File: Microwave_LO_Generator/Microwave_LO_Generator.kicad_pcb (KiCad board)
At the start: 2 copper layers, 41 parts, among them IC1 ADP150AUJZ-3.3-R7, J1 BNC_THT, J2 SMA_END, J3 SMA_END, U1 ADF4150HV, U2 LM317L_SO8, U3 LM317L_SO8, X1 IQXT-220-1

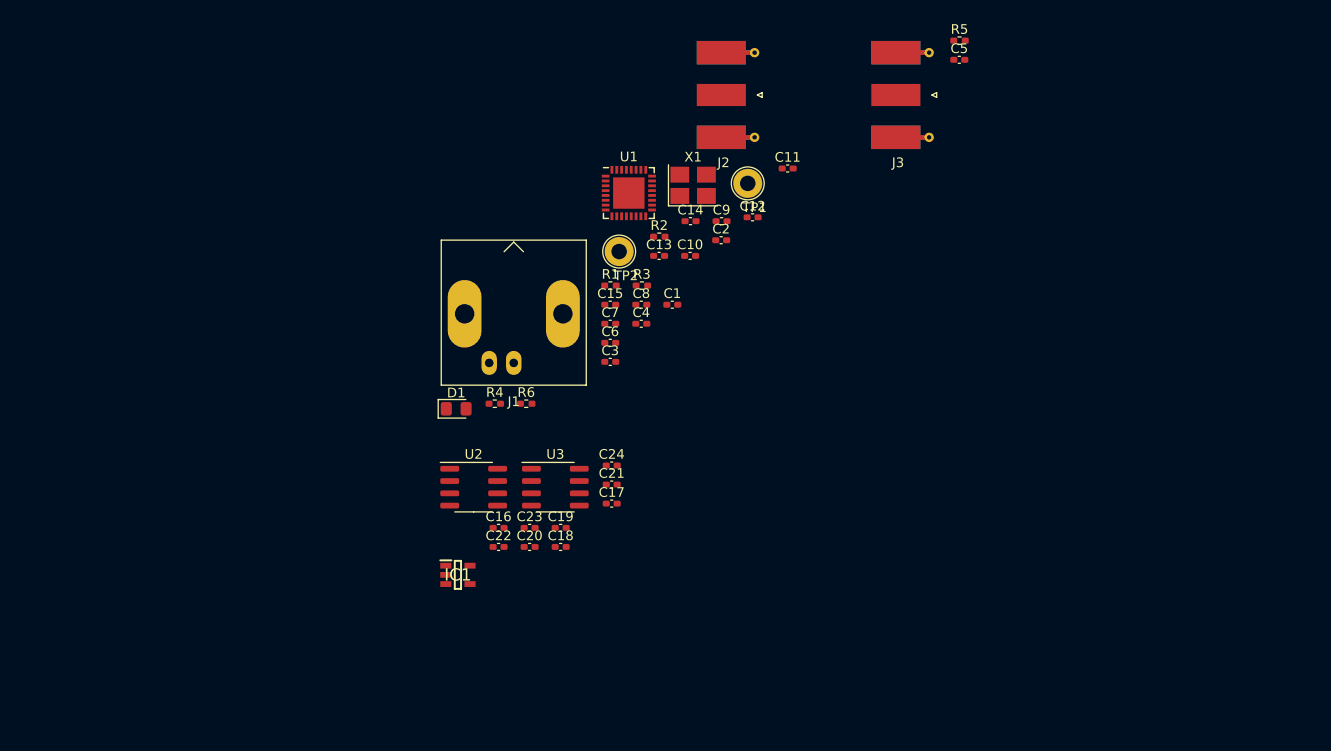
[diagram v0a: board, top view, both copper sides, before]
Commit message: add vco
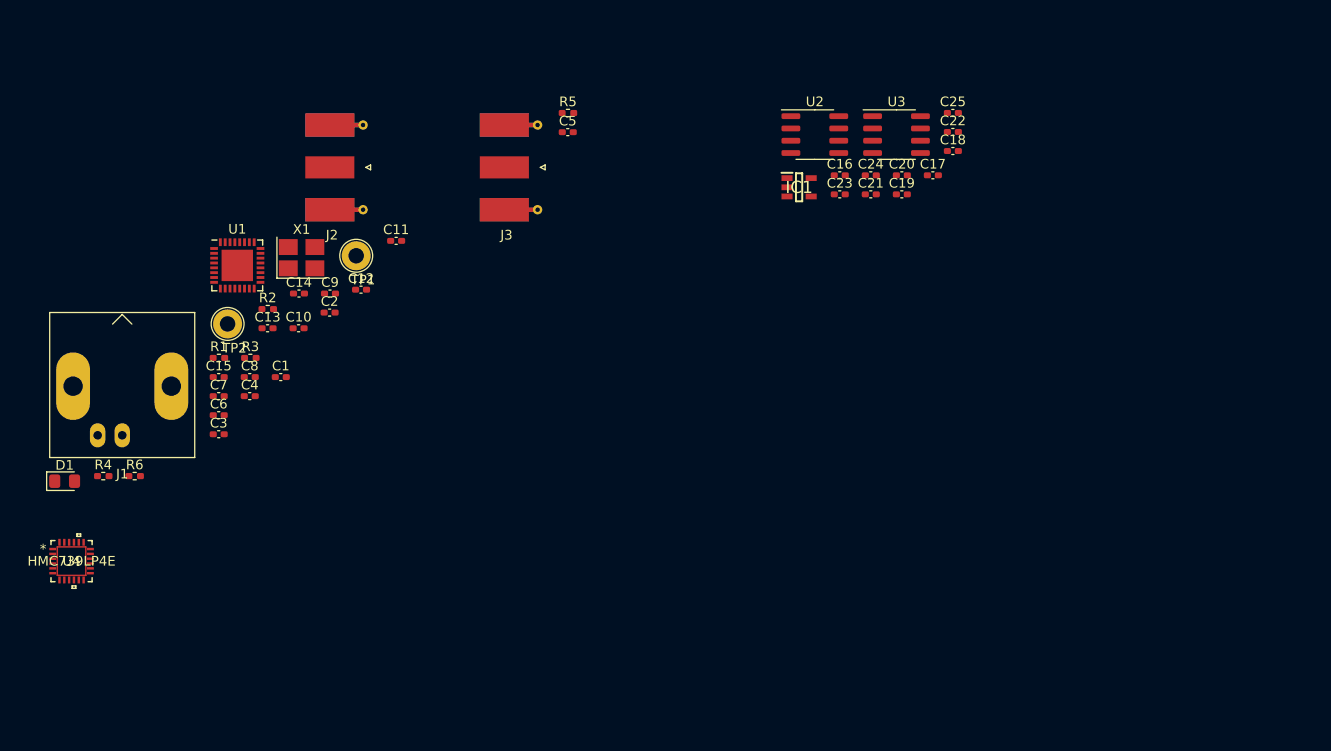
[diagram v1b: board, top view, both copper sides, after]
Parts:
- added C25: 1u, Capacitor_SMD:C_0402_1005Metric_Pad0.74x0.62mm_HandSolder, F.Cu at (236.0, 98.3)
- added U4: HMC739LP4E, Microwave_LO_Generator:HMC739LP4E, F.Cu at (144.9, 144.6)
- moved C22 63.6 mm to (236.0, 100.2)
- moved C18 57.6 mm to (236.0, 102.2)
- moved C20 54.4 mm to (230.7, 104.7)
- moved IC1 53.4 mm to (220.1, 106.0)
- moved C16 50.7 mm to (224.3, 104.7)
- moved U2 50.7 mm to (221.7, 100.5)
- moved U3 50.7 mm to (230.2, 100.5)
- moved C19 49.3 mm to (230.7, 106.7)
- moved C17 47.5 mm to (234.0, 104.7)
- moved C23 47.1 mm to (224.3, 106.7)
- moved C12 41.2 mm to (174.8, 116.6)
- moved D1 41.2 mm to (144.2, 136.4)
- moved J1 41.2 mm to (150.1, 131.6)
- moved R1 41.2 mm to (160.1, 123.6)
- moved R3 41.2 mm to (163.4, 123.6)
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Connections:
- net Net-(C15-Pad2) renamed CPout
- IC1 pad 4: Net-(IC1-Pad4) -> +5VD

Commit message: Update and fix
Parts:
- added C26: 100p, Capacitor_SMD:C_0402_1005Metric_Pad0.74x0.62mm_HandSolder, F.Cu at (263.5, 121.3)
- added C27: 4.7u, Capacitor_SMD:C_0402_1005Metric_Pad0.74x0.62mm_HandSolder, F.Cu at (262.3, 121.3)
- added C28: 1000p, Capacitor_SMD:C_0402_1005Metric_Pad0.74x0.62mm_HandSolder, F.Cu at (251.2, 118.0)
- added C29: 100p, Capacitor_SMD:C_0402_1005Metric_Pad0.74x0.62mm_HandSolder, F.Cu at (268.7, 116.2)
- added C30: 4.7u, Capacitor_SMD:C_0402_1005Metric_Pad0.74x0.62mm_HandSolder, F.Cu at (268.6, 114.3)
- added D2: DIODE, Diode_SMD:D_MELF, F.Cu at (202.1, 137.8)
- added D3: DIODE, Diode_SMD:D_MELF, F.Cu at (218.4, 134.6)
- added D4: DIODE, Diode_SMD:D_MELF, F.Cu at (218.4, 150.5)
- added D5: DIODE, Diode_SMD:D_MELF, F.Cu at (219.1, 142.9)
- added D6: DIODE, Diode_SMD:D_MELF, F.Cu at (219.1, 158.8)
- added D7: LED, LED_SMD:LED_0805_2012Metric_Pad1.15x1.40mm_HandSolder, F.Cu at (188.6, 147.3)
- added R10: 720r, Resistor_SMD:R_0402_1005Metric_Pad0.72x0.64mm_HandSolder, F.Cu at (224.8, 140.3)
- added R11: 240r, Resistor_SMD:R_0402_1005Metric_Pad0.72x0.64mm_HandSolder, F.Cu at (219.7, 156.2)
- added R12: 1K488, Resistor_SMD:R_0402_1005Metric_Pad0.72x0.64mm_HandSolder, F.Cu at (224.8, 156.2)
- added R13: 1K, Resistor_SMD:R_0402_1005Metric_Pad0.72x0.64mm_HandSolder, F.Cu at (187.3, 144.8)
- added R14: 51r, Resistor_SMD:R_0402_1005Metric_Pad0.72x0.64mm_HandSolder, F.Cu at (249.2, 117.4)
- added R15: 51r, Resistor_SMD:R_0402_1005Metric_Pad0.72x0.64mm_HandSolder, F.Cu at (267.3, 125.1)
- added R7: 0r, Resistor_SMD:R_0402_1005Metric_Pad0.72x0.64mm_HandSolder, F.Cu at (212.7, 132.1)
- added R8: 0r, Resistor_SMD:R_0402_1005Metric_Pad0.72x0.64mm_HandSolder, F.Cu at (212.7, 148.0)
- added R9: 240r, Resistor_SMD:R_0402_1005Metric_Pad0.72x0.64mm_HandSolder, F.Cu at (219.7, 140.3)
- C23: value 1u -> 4.7u
- C24: value 1u -> 100p
- moved U4 124.9 mm to (267.3, 120.0)
- moved R6 103.6 mm to (253.9, 120.5), turned to 180 degrees
- moved C15 96.5 mm to (256.5, 121.1), turned to 90 degrees
- moved D1 91.5 mm to (234.3, 120.7), turned to 90 degrees
- moved R4 89.2 mm to (235.6, 118.1)
- moved C6 88.2 mm to (247.3, 116.2), turned to 270 degrees
- moved C8 85.4 mm to (248.5, 119.3), turned to 180 degrees
- moved C7 84.6 mm to (242.6, 108.6)
- moved C13 83.4 mm to (248.5, 121.1), turned to 90 degrees
- moved C14 82.7 mm to (250.8, 123.6), turned to 90 degrees
- moved U1 80.1 mm to (241.9, 118.7), turned to 90 degrees
- moved R1 76.5 mm to (236.2, 115.6)
- moved C10 75.4 mm to (243.8, 122.6), turned to 180 degrees
- moved C4 75.0 mm to (237.5, 116.8), turned to 180 degrees
- moved R3 74.2 mm to (237.5, 121.3), turned to 270 degrees
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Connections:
- net Net-(C5-Pad2) renamed DIV16
- C1 pad 1: GND -> 0
- C10 pad 1: GND -> 0
- C11 pad 1: GND -> 0
- C12 pad 1: GND -> 0
- C13 pad 1: GND -> 0
- C14 pad 1: GND -> 0
- C15 pad 1: GND -> 0
- C2 pad 1: GND -> 0
- C21 pad 2: +5V -> +5VA
- C25 pad 2: Net-(C25-Pad2) -> +3V3
- C6 pad 1: GND -> 0
- C7 pad 1: GND -> 0
- C8 pad 1: GND -> 0
- C9 pad 1: GND -> 0
- D1 pad 1: GND -> 0
- IC1 pad 4: +5VD -> Net-(IC1-Pad4)
- IC1 pad 5: Net-(C25-Pad2) -> +3V3
- J1 pad 2: GND -> 0
- J2 pad 2: GND -> 0
- J3 pad 2: GND -> 0
- R2 pad 2: GND -> 0
- R3 pad 2: GND -> 0
- U1 pad 1: GND -> 0
- U1 pad 10: GND -> 0
- U1 pad 12: GND -> 0
- U1 pad 16: GND -> 0
- U1 pad 17: GND -> 0
- U1 pad 23: GND -> 0
- U1 pad 24: GND -> 0
- U1 pad 29: GND -> 0
- U1 pad 30: GND -> 0
- U1 pad 32: GND -> 0
- U1 pad 7: GND -> 0
- U1 pad 8: GND -> 0
- U2 pad 2: +5V -> +5VA
- U2 pad 3: +5V -> +5VA
- U2 pad 6: +5V -> +5VA
- U2 pad 7: +5V -> +5VA
- U4 pad 20: Net-(U4-Pad20) -> +5VA
- U4 pad 4: Net-(U4-Pad4) -> +5VD
- X1 pad 2: GND -> 0
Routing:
- net +9V: track 0.00 -> 21.6 mm
- net CPout: track 0.00 -> 17.9 mm, vias 0 -> 2
- net +3V3: track 0.00 -> 15.3 mm, vias 0 -> 1
- net +5VA: track 0.00 -> 14.6 mm
- net Net-(C28-Pad2): track 0.00 -> 14.1 mm
- net +5VD: track 0.00 -> 10.1 mm
- net Net-(C18-Pad2): track 0.00 -> 10.0 mm
- net Net-(C17-Pad2): track 0.00 -> 10.0 mm
- net Net-(C20-Pad2): track 0.00 -> 9.80 mm
- net Net-(C19-Pad2): track 0.00 -> 9.46 mm
- net 0: track 0.00 -> 9.20 mm
- net Net-(C13-Pad2): track 0.00 -> 9.03 mm
- net DIV16: track 0.00 -> 6.34 mm
- net Net-(R1-Pad1): track 0.00 -> 4.34 mm
- net Net-(R4-Pad2): track 0.00 -> 3.61 mm
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
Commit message: Update PCB
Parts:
- removed C3: 1n, Capacitor_SMD:C_0402_1005Metric_Pad0.74x0.62mm_HandSolder
- removed C5: 100p, Capacitor_SMD:C_0402_1005Metric_Pad0.74x0.62mm_HandSolder
- removed J1: BNC_THT, Connector_Coaxial:BNC_Amphenol_B6252HB-NPP3G-50_Horizontal
- removed J2, J3: SMA_END, Connector_Coaxial:SMA_Molex_73251-1153_EdgeMount_Horizontal
- removed TP1, TP2: TestPoint, TestPoint:TestPoint_Loop_D2.60mm_Drill1.6mm_Beaded
- moved C23 68.6 mm to (233.7, 104.1), turned to 0 degrees
- moved C24 65.9 mm to (233.7, 106.0), turned to 0 degrees
- moved D7 62.8 mm to (237.5, 108.0), turned to 0 degrees
- moved R13 61.3 mm to (238.1, 110.5), turned to 90 degrees
- moved IC1 60.5 mm to (233.0, 109.9), turned to 270 degrees
- moved D5 59.7 mm to (261.6, 101.0), turned to 0 degrees
- moved R7 58.9 mm to (268.0, 111.8), turned to 0 degrees
- moved C25 58.2 mm to (236.2, 110.5), turned to 270 degrees
- moved R9 55.3 mm to (261.0, 103.5), turned to 180 degrees
- moved C17 54.6 mm to (265.4, 111.1), turned to 270 degrees
- moved D3 50.6 mm to (262.3, 109.2), turned to 270 degrees
- moved C19 50.2 mm to (255.9, 102.2), turned to 0 degrees
- moved R10 48.3 mm to (255.9, 103.5), turned to 180 degrees
- moved U2 42.7 mm to (255.9, 107.3), turned to 180 degrees
- moved C21 38.0 mm to (250.8, 106.0), turned to 270 degrees
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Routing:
- net 0: track 9.20 -> 101.6 mm
- net +5VD: track 10.1 -> 67.5 mm, vias 0 -> 2
- net +12V: track 0.00 -> 57.2 mm, vias 0 -> 2
- net +3V3: track 15.3 -> 66.8 mm, vias 1 -> 3
- net +5VA: track 14.6 -> 36.5 mm
- net +9V: track 21.6 -> 27.5 mm
- net Net-(U1-Pad21): track 0.00 -> 2.72 mm, vias 0 -> 1
- net Net-(R15-Pad1): track 0.00 -> 2.64 mm
- net Net-(C20-Pad2): track 9.80 -> 11.3 mm
- net Net-(C13-Pad2): track 9.03 -> 9.82 mm
- net Net-(C6-Pad2): track 3.26 -> 3.79 mm
- net CPout: track 17.9 -> 18.4 mm
- added copper zone on F.Cu, net +5VA
- added copper zone on F.Cu, net +9V
- added copper zone on B.Cu, net 0
- added copper zone on F.Cu, net 0
- added copper zone on In1.Cu, net 0
- added copper zone on In2.Cu, net 0
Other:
- copper layers 2 -> 4
- net class CPWG added: clearance 0.2, trace_width 0.448177, via_dia 0.8, via_drill 0.4
- net class Default: trace_width 0.25 -> 0.3
- rule via_min_drill: 0.3 -> 0.2
- rule via_min_size: 0.4 -> 0.5

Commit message: Update
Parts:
- added J4: Conn_01x05_Male, Connector_PinHeader_2.54mm:PinHeader_1x05_P2.54mm_Vertical, F.Cu at (230.5, 125.7)
- added R16: 0, Resistor_SMD:R_0402_1005Metric_Pad0.72x0.64mm_HandSolder, F.Cu at (242.4, 113.7)
- added R17: DNI, Resistor_SMD:R_0603_1608Metric_Pad0.98x0.95mm_HandSolder, F.Cu at (240.8, 114.9)
- moved C16 4.45 mm to (231.1, 134.0)
- moved D2 4.45 mm to (227.5, 134.0)
- moved R8 4.45 mm to (231.1, 128.9)
- moved C18 4.44 mm to (233.7, 129.5)
- moved C20 4.44 mm to (243.2, 138.4)
- moved C22 4.44 mm to (248.3, 134.6)
- moved D4 4.44 mm to (236.9, 131.4)
- moved D6 4.44 mm to (237.5, 139.7)
- moved R11 4.44 mm to (238.1, 137.2)
- moved R12 4.44 mm to (243.2, 137.2)
- moved U3 4.44 mm to (243.2, 133.3)
- moved C7 1.42 mm to (252.7, 121.3)
- moved R2 1.38 mm to (237.6, 114.2)
- moved R6 1.27 mm to (253.9, 123.1)
- moved C13 1.27 mm to (248.5, 123.6)
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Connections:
- U1 pad 33: (no net) -> 0
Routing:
- net 0: track 101.6 -> 60.1 mm, vias 0 -> 27
- net +12V: track 57.2 -> 70.8 mm
- net +5VD: track 67.5 -> 78.0 mm
- net Net-(J4-Pad2): track 0.00 -> 9.98 mm
- net Net-(J4-Pad3): track 0.00 -> 8.39 mm
- net +3V3: track 66.8 -> 73.6 mm
- net Net-(J4-Pad4): track 0.00 -> 6.80 mm
- net CPout: track 18.4 -> 24.2 mm
- net Net-(J4-Pad5): track 0.00 -> 5.21 mm
- net +5VA: track 36.5 -> 31.8 mm
- net Net-(C4-Pad1): track 3.49 -> 4.78 mm
- net Net-(C6-Pad2): track 3.79 -> 5.06 mm
- net +9V: track 27.5 -> 28.7 mm
- net Net-(C13-Pad2): track 9.82 -> 10.4 mm
- net Net-(R16-Pad2): track 2.72 -> 3.17 mm, vias 1 -> 0
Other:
- board outline added: 49.5 x 47 mm
- rule trace_min: 0.2 -> 0.19
